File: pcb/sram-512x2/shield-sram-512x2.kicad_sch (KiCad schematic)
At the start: 12 parts, among them U1 IS61WV25616-10TLI, U2 IS61WV25616-10TLI

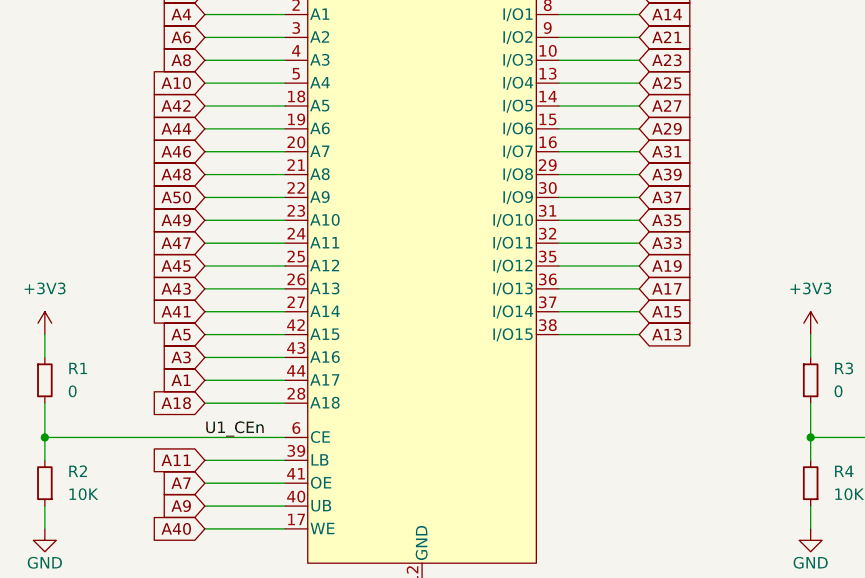
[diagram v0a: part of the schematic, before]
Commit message: [sram][scripts][pins] update 512 sram to avoid pll pin
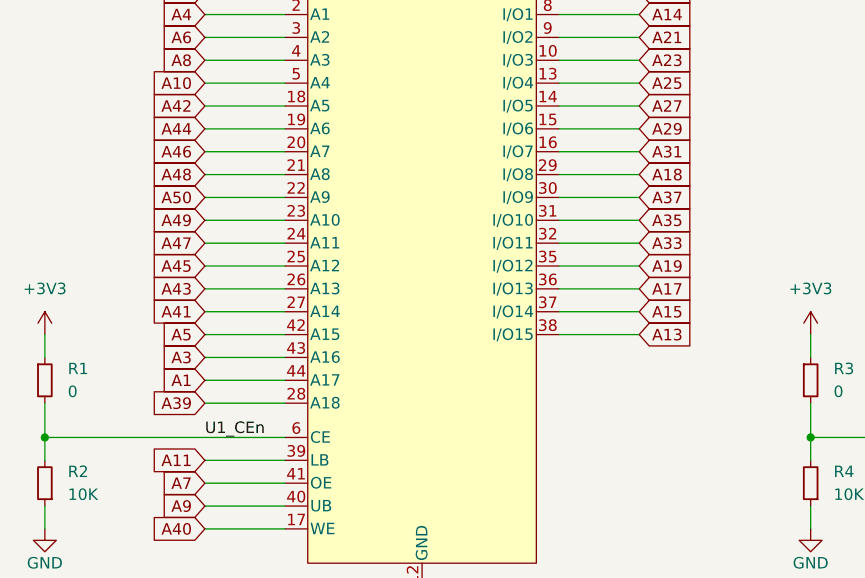
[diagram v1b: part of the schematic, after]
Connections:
- net A18: now also U1.29 (I/O8); no longer U1.28 (A18)
- net A39: now also U1.28 (A18); no longer U1.29 (I/O8)

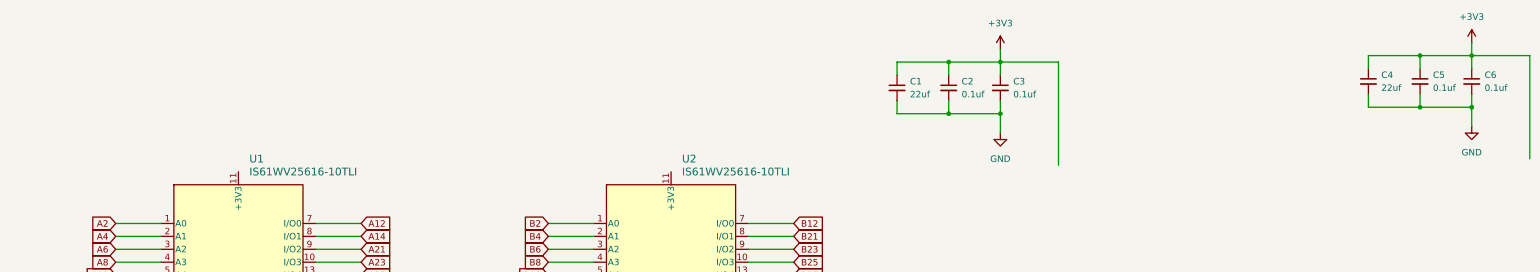
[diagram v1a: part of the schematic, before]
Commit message: [sram] fix disconnected decoupling
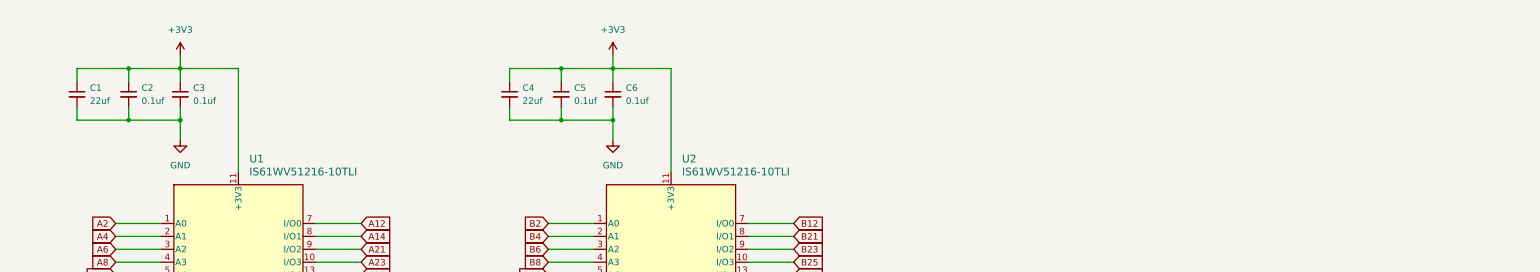
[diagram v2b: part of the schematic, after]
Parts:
- U1, U2: value IS61WV25616-10TLI -> IS61WV51216-10TLI; Digi-Key Part Number 706-1146-ND -> 706-1107-ND; LCSC Part # C883296 -> C397874
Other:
- moved on the sheet: C1, C2, C3, C4, C5, C6
